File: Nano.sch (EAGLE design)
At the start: 25 parts

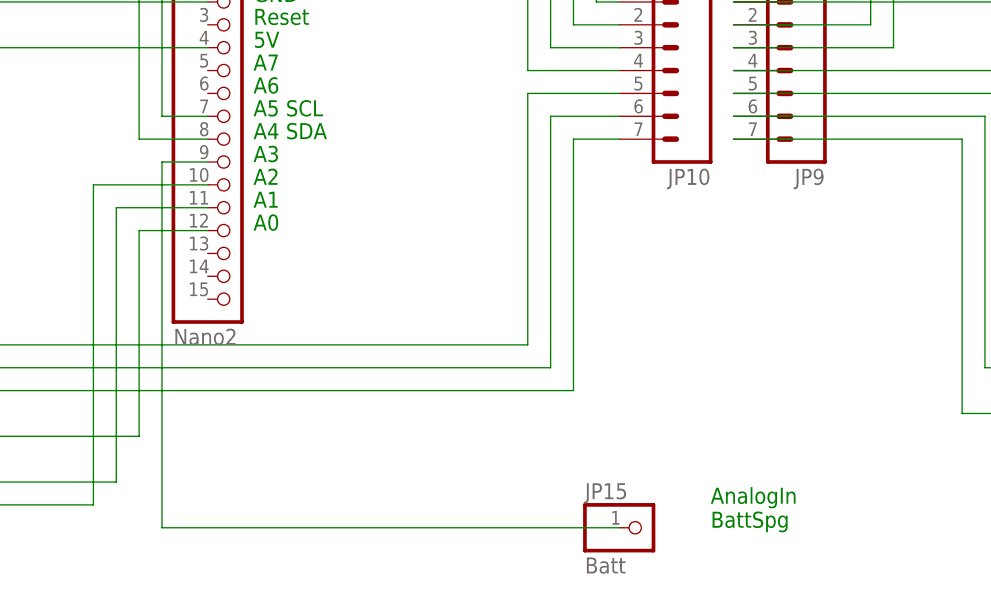
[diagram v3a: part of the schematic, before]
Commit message: 
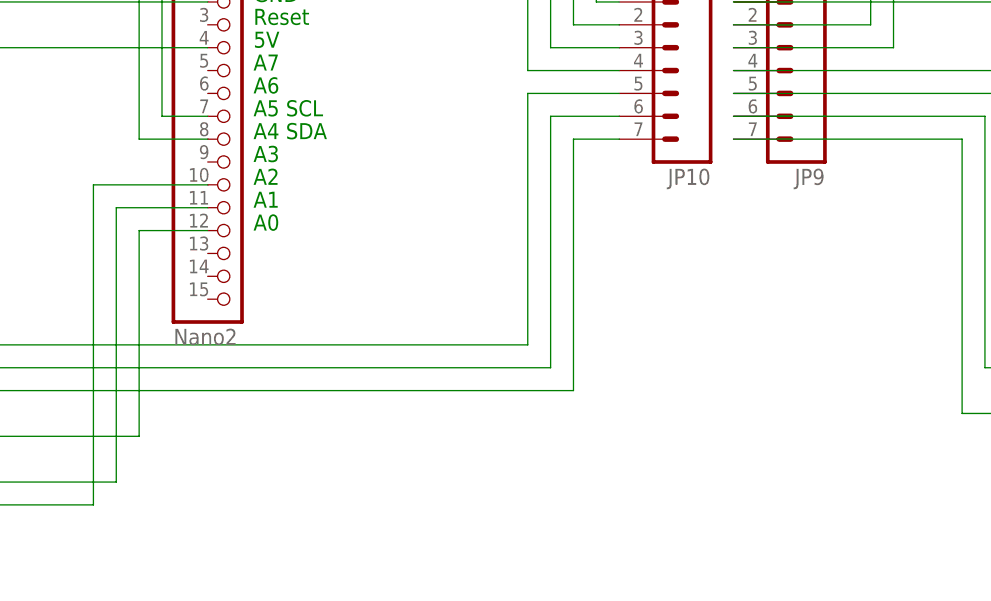
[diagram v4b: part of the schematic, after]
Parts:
- removed JP15: Batt, pinhead:PINHD-1X1
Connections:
- removed net N$6: JP15.1, JP2.9
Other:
- note removed: "AnalogIn BattSpg"
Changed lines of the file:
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@@
 <part name="JP14" library="SparkFun-Connectors" deviceset="M02" device="LOCK" value="I2C"/>
 <part name="JP9" library="SparkFun-Connectors" deviceset="M07" device="" value="Tast"/>
-<part name="JP15" library="pinhead" deviceset="PINHD-1X1" device="" value="Batt"/>
 <part name="FRAME1" library="SparkFun-Aesthetics" deviceset="FRAME-A4L" device=""/>
 </parts>
@@
 2-blau
 1-schwarz</text>
-<text x="121.92" y="12.7" size="1.778" layer="91">AnalogIn
-BattSpg</text>
 </plain>
 <instances>
@@
 <instance part="JP14" gate="G$1" x="58.42" y="142.24" rot="R270"/>
 <instance part="JP9" gate="G$1" x="129.54" y="66.04" rot="R180"/>
-<instance part="JP15" gate="G$1" x="114.3" y="12.7"/>
 <instance part="FRAME1" gate="G$1" x="-53.34" y="-20.32"/>
 </instances>
@@
 </segment>
 </net>
-<net name="N$6" class="0">
-<segment>
-<pinref part="JP15" gate="G$1" pin="1"/>
-<wire x1="111.76" y1="12.7" x2="60.96" y2="12.7" width="0.1524" layer="91"/>
-<pinref part="JP2" gate="A" pin="9"/>
-<wire x1="66.04" y1="53.34" x2="60.96" y2="53.34" width="0.1524" layer="91"/>
-<wire x1="60.96" y1="53.34" x2="60.96" y2="12.7" width="0.1524" layer="91"/>
-</segment>
-</net>
